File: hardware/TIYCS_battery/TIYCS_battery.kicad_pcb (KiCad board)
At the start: 2 copper layers, 100 x 100 mm, 27 parts, among them J1 Barrel_Jack_Switch, J2 External Jack, J3 pinHeaders, U1 4S_BMS, U2 4_18650, U3 XL4015

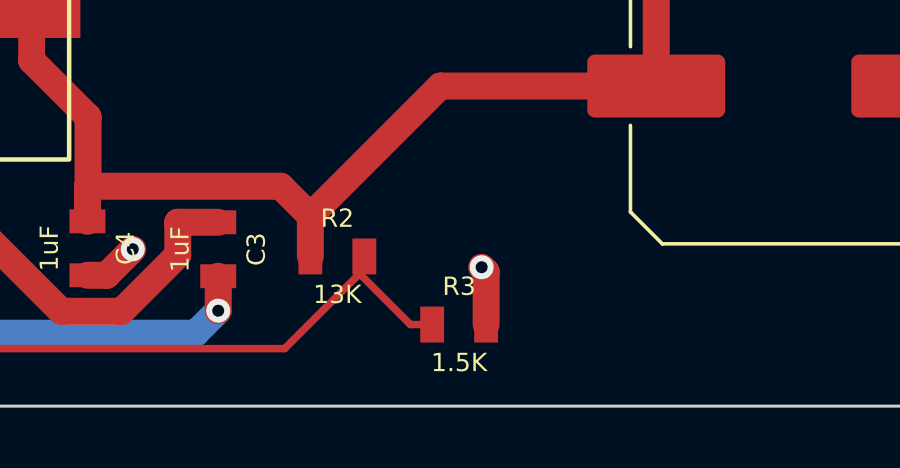
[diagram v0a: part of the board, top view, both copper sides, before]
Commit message: Fixboard for 3.3V regulator
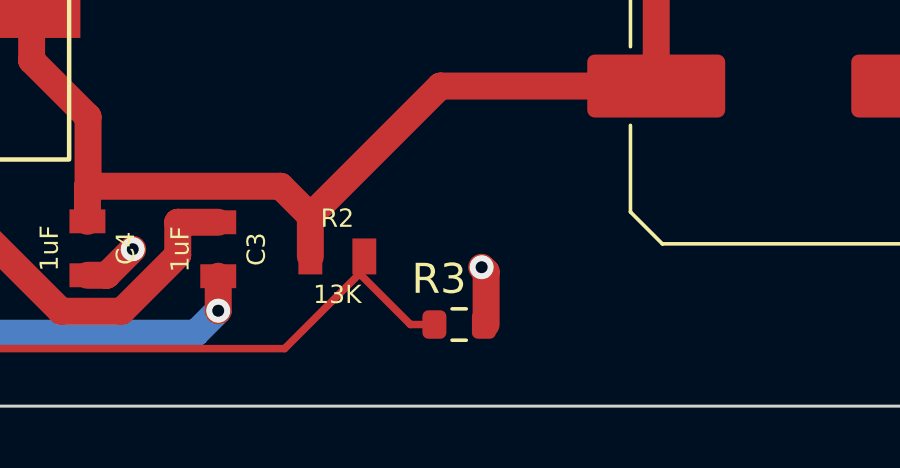
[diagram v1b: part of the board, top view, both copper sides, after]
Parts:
- R3: footprint Resistors:0805 -> Resistor_SMD:R_0603_1608Metric
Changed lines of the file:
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@@
       (net 3 "Net-(C3-Pad2)") (pintype "passive") (solder_mask_margin 0.1016))
   )
-  (footprint "Resistors:0805" (layer "F.Cu")
+  (footprint "Resistor_SMD:R_0603_1608Metric" (layer "F.Cu")
     (at 74.03 97.28)
-    (descr "GENERIC 2012 (0805) PACKAGE")
-    (tags "GENERIC 2012 (0805) PACKAGE")
+    (descr "Resistor SMD 0603 (1608 Metric), square (rectangular) end terminal, IPC_7351 nominal, (Body size source: IPC-SM-782 page 72, https://www.pcb-3d.com/wordpress/wp-content/uploads/ipc-sm-782a_amendment_1_and_2.pdf), generated with kicad-footprint-generator")
+    (tags "resistor")
     (property "Field4" "C26010")
     (property "Sheetfile" "TIYCS_battery.kicad_sch")
     (property "Sheetname" "")
     (attr smd)
-    (fp_text reference "R3" (at 0 -1.27) (layer "F.SilkS")
-      (effects (font (size 0.6096 0.6096) (thickness 0.127)))
+    (fp_text reference "R3" (at -0.67 -1.52) (layer "F.SilkS")
+      (effects (font (size 1 1) (thickness 0.15)))
     )
-    (fp_text value "1.5K" (at 0 1.27) (layer "F.SilkS")
-      (effects (font (size 0.6096 0.6096) (thickness 0.127)))
+    (fp_text value "1.5K" (at 0 1.43) (layer "F.Fab")
+      (effects (font (size 1 1) (thickness 0.15)))
     )
-    (fp_line (start 1.4986 0.79756) (end -1.4986 0.79756) (layer "F.CrtYd") (width 0.0508))
-    (fp_line (start 1.4986 -0.79756) (end 1.4986 0.79756) (layer "F.CrtYd") (width 0.0508))
-    (fp_line (start -1.4986 0.79756) (end -1.4986 -0.79756) (layer "F.CrtYd") (width 0.0508))
-    (fp_line (start -1.4986 -0.79756) (end 1.4986 -0.79756) (layer "F.CrtYd") (width 0.0508))
-    (pad "1" smd rect locked (at -0.89916 0) (size 0.79756 1.19888) (layers "F.Cu" "F.Paste" "F.Mask")
-      (net 13 "Net-(R2-Pad2)") (pintype "passive") (solder_mask_margin 0.1016))
-    (pad "2" smd rect locked (at 0.89916 0) (size 0.79756 1.19888) (layers "F.Cu" "F.Paste" "F.Mask")
-      (net 2 "GND") (pintype "passive") (solder_mask_margin 0.1016))
+    (fp_text user "${REFERENCE}" (at 0 0) (layer "F.Fab")
+      (effects (font (size 0.4 0.4) (thickness 0.06)))
+    )
+    (fp_line (start -0.237258 0.5225) (end 0.237258 0.5225) (layer "F.SilkS") (width 0.12))
+    (fp_line (start -0.237258 -0.5225) (end 0.237258 -0.5225) (layer "F.SilkS") (width 0.12))
+    (fp_line (start -1.48 0.73) (end -1.48 -0.73) (layer "F.CrtYd") (width 0.05))
+    (fp_line (start 1.48 0.73) (end -1.48 0.73) (layer "F.CrtYd") (width 0.05))
+    (fp_line (start 1.48 -0.73) (end 1.48 0.73) (layer "F.CrtYd") (width 0.05))
+    (fp_line (start -1.48 -0.73) (end 1.48 -0.73) (layer "F.CrtYd") (width 0.05))
+    (fp_line (start 0.8 0.4125) (end -0.8 0.4125) (layer "F.Fab") (width 0.1))
+    (fp_line (start -0.8 0.4125) (end -0.8 -0.4125) (layer "F.Fab") (width 0.1))
+    (fp_line (start -0.8 -0.4125) (end 0.8 -0.4125) (layer "F.Fab") (width 0.1))
+    (fp_line (start 0.8 -0.4125) (end 0.8 0.4125) (layer "F.Fab") (width 0.1))
+    (pad "1" smd roundrect locked (at -0.825 0) (size 0.8 0.95) (layers "F.Cu" "F.Paste" "F.Mask") (roundrect_rratio 0.25)
+      (net 13 "Net-(R2-Pad2)") (pintype "passive"))
+    (pad "2" smd roundrect locked (at 0.825 0) (size 0.8 0.95) (layers "F.Cu" "F.Paste" "F.Mask") (roundrect_rratio 0.25)
+      (net 2 "GND") (pintype "passive"))
+    (model "${KICAD6_3DMODEL_DIR}/Resistor_SMD.3dshapes/R_0603_1608Metric.wrl"
+      (offset (xyz 0 0 0))
+      (scale (xyz 1 1 1))
+      (rotate (xyz 0 0 0))
+    )
   )
   (footprint "Connector_BarrelJack:BarrelJack_CLIFF_FC681465S_SMT_Horizontal" (layer "F.Cu")

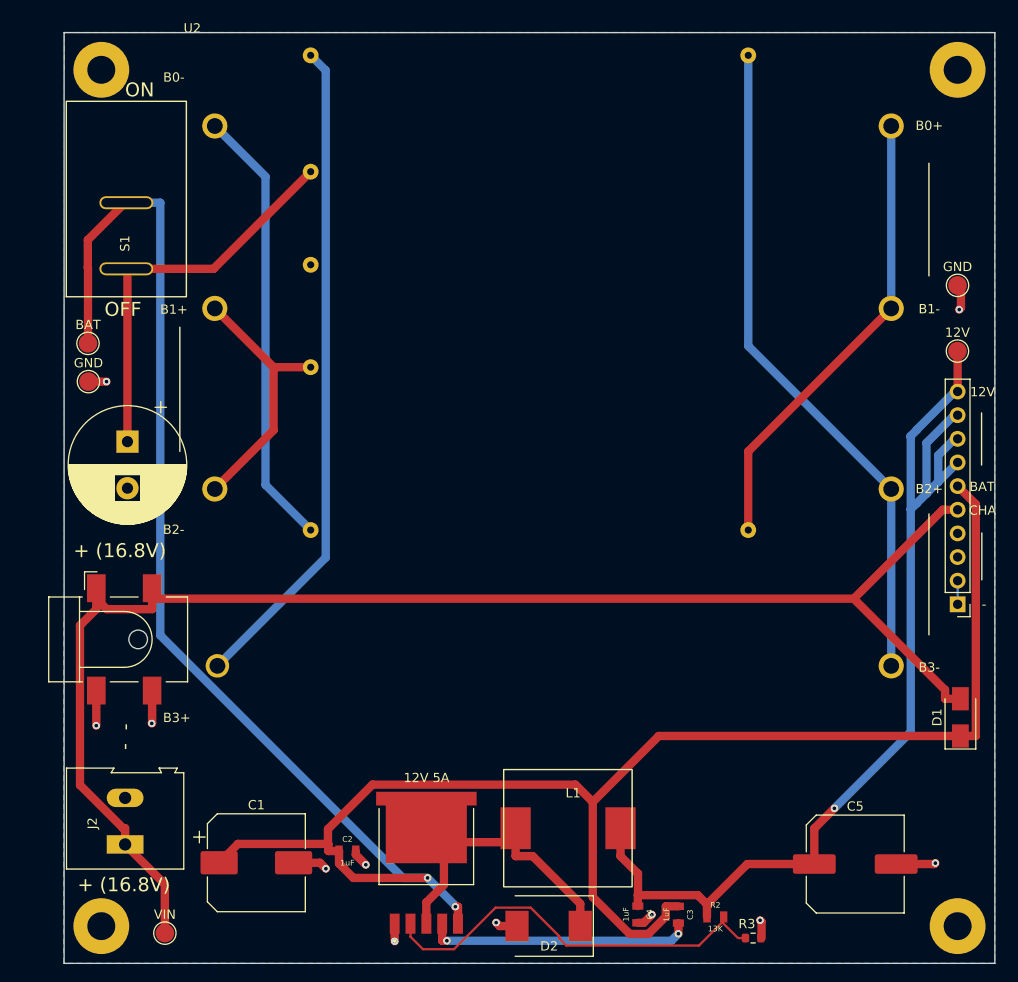
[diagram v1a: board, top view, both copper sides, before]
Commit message: Added XT60 conn to battery board
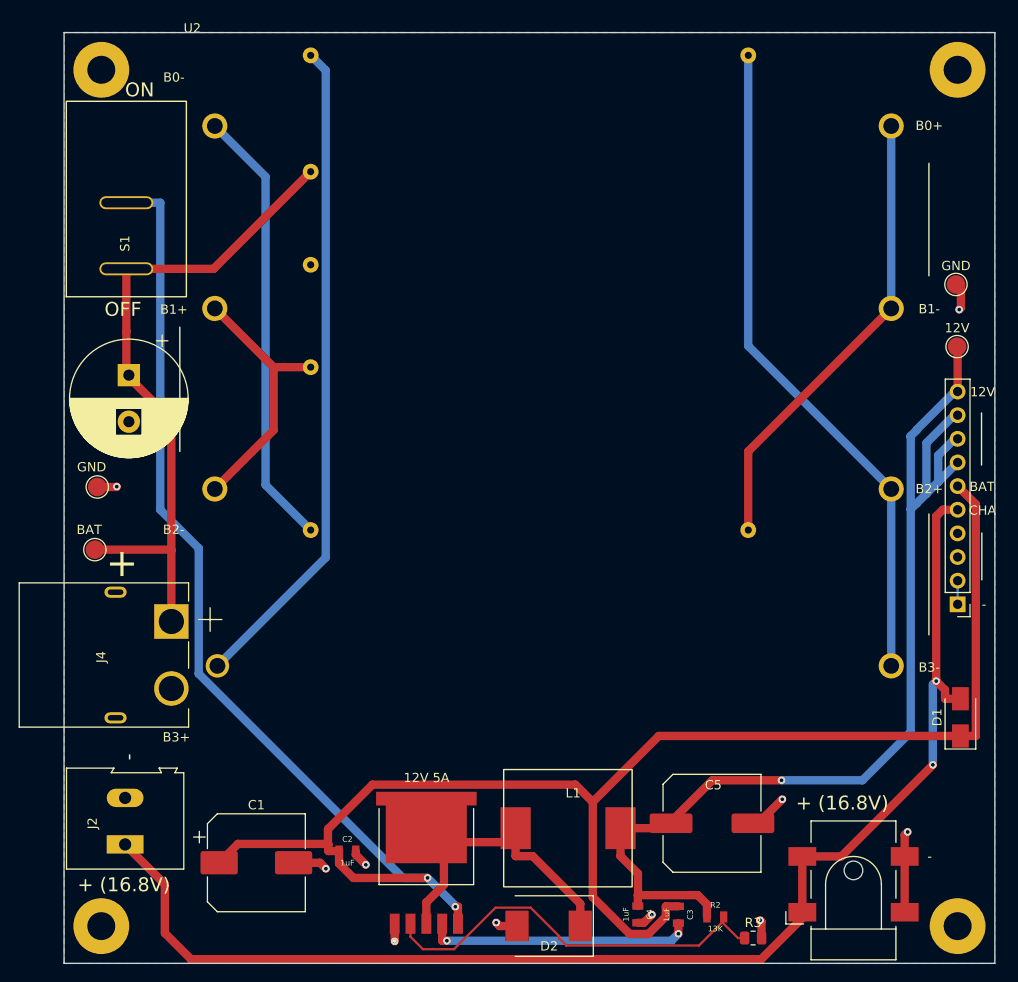
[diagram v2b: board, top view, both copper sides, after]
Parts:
- removed the GND at (96.0, 27.2)
- removed the GND at (2.62, 37.5)
- removed VIN: TestPoint_Pad_D2.0mm, TestPoint:TestPoint_Pad_D2.0mm
- added GND: TestPoint_Pad_D2.0mm, TestPoint:TestPoint_Pad_D2.0mm, F.Cu at (3.57, 48.8)
- added GND: TestPoint_Pad_D2.0mm, TestPoint:TestPoint_Pad_D2.0mm, F.Cu at (95.8, 27.1)
- added J4: XT60PW-M, XT60PW-M:AMASS_XT60PW-M, F.Cu at (5.53, 66.9)
- R3: footprint Resistor_SMD:R_0603_1608Metric -> Resistor_SMD:R_0805_2012Metric
- moved J1 82.7 mm to (84.8, 91.5), turned to 90 degrees
- moved BAT 22.2 mm to (3.31, 55.5)
- moved C5 16.0 mm to (69.6, 85.0)
- moved C6 7.15 mm to (6.96, 36.8)
- moved 12V 0.48 mm to (95.9, 33.7)
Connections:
- 12V pad 1: +12V -> (no net)
- BAT pad 1: V_SENSE_BAT -> Net-(C6-Pad1)
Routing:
- net Net-(C6-Pad1): track 42.7 -> 72.3 mm
- net V_SENSE: track 157.4 -> 140.2 mm, vias 0 -> 2
- net V_SENSE_BAT: track 266.2 -> 249.5 mm
- net +12V: track 116.3 -> 119.4 mm
- net GND: track 33.6 -> 34.6 mm, vias 11 -> 10
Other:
- board text added: "+"

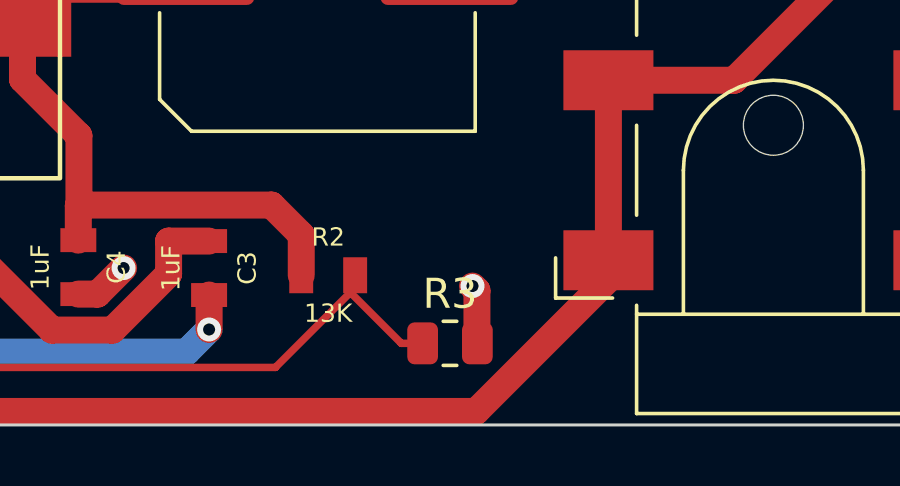
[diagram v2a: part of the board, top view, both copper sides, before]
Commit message: Battery PCB new gerber
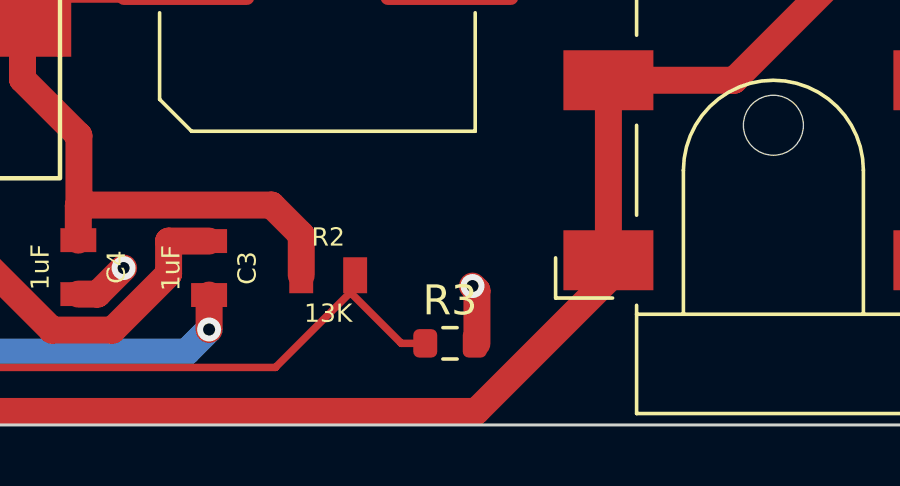
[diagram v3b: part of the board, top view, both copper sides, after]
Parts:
- R3: footprint Resistor_SMD:R_0805_2012Metric -> Resistor_SMD:R_0603_1608Metric
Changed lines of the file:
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@@
       (net 3 "Net-(C3-Pad2)") (pintype "passive") (solder_mask_margin 0.1016))
   )
-  (footprint "Resistor_SMD:R_0805_2012Metric" (layer "F.Cu")
+  (footprint "Resistor_SMD:R_0603_1608Metric" (layer "F.Cu")
     (at 74.03 97.28)
-    (descr "Resistor SMD 0805 (2012 Metric), square (rectangular) end terminal, IPC_7351 nominal, (Body size source: IPC-SM-782 page 72, https://www.pcb-3d.com/wordpress/wp-content/uploads/ipc-sm-782a_amendment_1_and_2.pdf), generated with kicad-footprint-generator")
+    (descr "Resistor SMD 0603 (1608 Metric), square (rectangular) end terminal, IPC_7351 nominal, (Body size source: IPC-SM-782 page 72, https://www.pcb-3d.com/wordpress/wp-content/uploads/ipc-sm-782a_amendment_1_and_2.pdf), generated with kicad-footprint-generator")
     (tags "resistor")
     (property "Field4" "C26010")
@@
     (property "Sheetname" "")
     (attr smd)
-    (fp_text reference "R3" (at 0 -1.65) (layer "F.SilkS")
+    (fp_text reference "R3" (at 0 -1.43) (layer "F.SilkS")
       (effects (font (size 1 1) (thickness 0.15)))
     )
-    (fp_text value "1.5K" (at 0 1.65) (layer "F.Fab")
+    (fp_text value "1.5K" (at 0 1.43) (layer "F.Fab")
       (effects (font (size 1 1) (thickness 0.15)))
     )
     (fp_text user "${REFERENCE}" (at 0 0) (layer "F.Fab")
-      (effects (font (size 0.5 0.5) (thickness 0.08)))
+      (effects (font (size 0.4 0.4) (thickness 0.06)))
     )
-    (fp_line (start -0.227064 -0.735) (end 0.227064 -0.735) (layer "F.SilkS") (width 0.12))
-    (fp_line (start -0.227064 0.735) (end 0.227064 0.735) (layer "F.SilkS") (width 0.12))
-    (fp_line (start 1.68 -0.95) (end 1.68 0.95) (layer "F.CrtYd") (width 0.05))
-    (fp_line (start -1.68 -0.95) (end 1.68 -0.95) (layer "F.CrtYd") (width 0.05))
-    (fp_line (start 1.68 0.95) (end -1.68 0.95) (layer "F.CrtYd") (width 0.05))
-    (fp_line (start -1.68 0.95) (end -1.68 -0.95) (layer "F.CrtYd") (width 0.05))
-    (fp_line (start 1 0.625) (end -1 0.625) (layer "F.Fab") (width 0.1))
-    (fp_line (start -1 -0.625) (end 1 -0.625) (layer "F.Fab") (width 0.1))
-    (fp_line (start -1 0.625) (end -1 -0.625) (layer "F.Fab") (width 0.1))
-    (fp_line (start 1 -0.625) (end 1 0.625) (layer "F.Fab") (width 0.1))
-    (pad "1" smd roundrect locked (at -0.9125 0) (size 1.025 1.4) (layers "F.Cu" "F.Paste" "F.Mask") (roundrect_rratio 0.243902)
+    (fp_line (start -0.237258 -0.5225) (end 0.237258 -0.5225) (layer "F.SilkS") (width 0.12))
+    (fp_line (start -0.237258 0.5225) (end 0.237258 0.5225) (layer "F.SilkS") (width 0.12))
+    (fp_line (start 1.48 0.73) (end -1.48 0.73) (layer "F.CrtYd") (width 0.05))
+    (fp_line (start -1.48 0.73) (end -1.48 -0.73) (layer "F.CrtYd") (width 0.05))
+    (fp_line (start 1.48 -0.73) (end 1.48 0.73) (layer "F.CrtYd") (width 0.05))
+    (fp_line (start -1.48 -0.73) (end 1.48 -0.73) (layer "F.CrtYd") (width 0.05))
+    (fp_line (start 0.8 0.4125) (end -0.8 0.4125) (layer "F.Fab") (width 0.1))
+    (fp_line (start -0.8 0.4125) (end -0.8 -0.4125) (layer "F.Fab") (width 0.1))
+    (fp_line (start 0.8 -0.4125) (end 0.8 0.4125) (layer "F.Fab") (width 0.1))
+    (fp_line (start -0.8 -0.4125) (end 0.8 -0.4125) (layer "F.Fab") (width 0.1))
+    (pad "1" smd roundrect locked (at -0.825 0) (size 0.8 0.95) (layers "F.Cu" "F.Paste" "F.Mask") (roundrect_rratio 0.25)
       (net 13 "Net-(R2-Pad2)") (pintype "passive"))
-    (pad "2" smd roundrect locked (at 0.9125 0) (size 1.025 1.4) (layers "F.Cu" "F.Paste" "F.Mask") (roundrect_rratio 0.243902)
+    (pad "2" smd roundrect locked (at 0.825 0) (size 0.8 0.95) (layers "F.Cu" "F.Paste" "F.Mask") (roundrect_rratio 0.25)
       (net 2 "GND") (pintype "passive"))
-    (model "${KICAD6_3DMODEL_DIR}/Resistor_SMD.3dshapes/R_0805_2012Metric.wrl"
+    (model "${KICAD6_3DMODEL_DIR}/Resistor_SMD.3dshapes/R_0603_1608Metric.wrl"
       (offset (xyz 0 0 0))
       (scale (xyz 1 1 1))
